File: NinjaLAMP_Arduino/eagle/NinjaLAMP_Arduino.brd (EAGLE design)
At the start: 50.8 x 33 mm, 13 parts

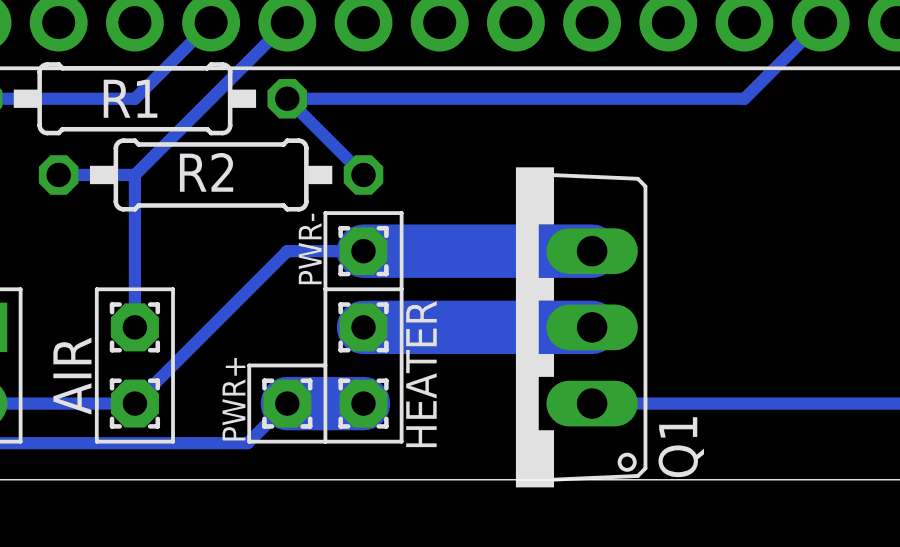
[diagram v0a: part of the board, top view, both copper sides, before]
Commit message: update 3d model : add cover
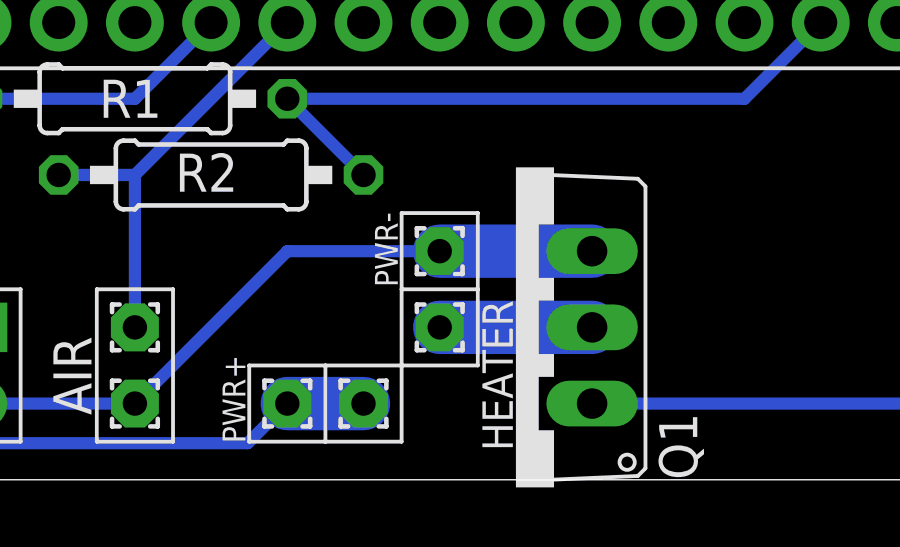
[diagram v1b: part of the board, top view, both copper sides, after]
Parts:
- moved HEATER2 2.54 mm to (20.3, 5.08)
- moved POWER- 2.54 mm to (20.3, 7.62)
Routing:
- net DRAIN: track 7.62 -> 5.08 mm
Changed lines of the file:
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@@
 <setting verticaltext="up"/>
 </settings>
-<grid distance="1" unitdist="mil" unit="mil" style="lines" multiple="1" display="yes" altdistance="5" altunitdist="mil" altunit="mil"/>
+<grid distance="50" unitdist="mil" unit="mil" style="lines" multiple="1" display="yes" altdistance="5" altunitdist="mil" altunit="mil"/>
 <layers>
 <layer number="1" name="Top" color="4" fill="1" visible="yes" active="yes"/>
@@
 <text x="3.556" y="1.4732" size="1.27" layer="25" rot="R90">WELL</text>
 <text x="8.7122" y="2.159" size="1.27" layer="25" rot="R90">AIR</text>
-<text x="16.383" y="6.4262" size="0.762" layer="25" rot="R90">PWR-</text>
-<text x="20.2184" y="0.9652" size="1.016" layer="25" rot="R90">HEATER</text>
+<text x="18.923" y="6.4262" size="0.762" layer="25" rot="R90">PWR-</text>
+<text x="22.7584" y="0.9652" size="1.016" layer="25" rot="R90">HEATER</text>
 <wire x1="8.89" y1="6.35" x2="8.89" y2="1.27" width="0.127" layer="21"/>
 <wire x1="8.89" y1="1.27" x2="11.43" y2="1.27" width="0.127" layer="21"/>
@@
 <wire x1="11.43" y1="1.27" x2="11.43" y2="6.35" width="0.127" layer="21"/>
 <wire x1="16.51" y1="1.27" x2="19.05" y2="1.27" width="0.127" layer="21"/>
-<wire x1="19.05" y1="1.27" x2="19.05" y2="6.35" width="0.127" layer="21"/>
-<wire x1="19.05" y1="6.35" x2="16.51" y2="6.35" width="0.127" layer="21"/>
-<wire x1="16.51" y1="6.35" x2="16.51" y2="3.81" width="0.127" layer="21"/>
+<wire x1="19.05" y1="1.27" x2="19.05" y2="3.81" width="0.127" layer="21"/>
+<wire x1="19.05" y1="3.81" x2="19.05" y2="6.35" width="0.127" layer="21"/>
 <wire x1="16.51" y1="3.81" x2="16.51" y2="1.27" width="0.127" layer="21"/>
 <wire x1="12.7" y1="22.86" x2="2.54" y2="22.86" width="0.127" layer="21"/>
@@
 <wire x1="13.97" y1="1.27" x2="13.97" y2="3.81" width="0.127" layer="21"/>
 <wire x1="13.97" y1="3.81" x2="16.51" y2="3.81" width="0.127" layer="21"/>
-<wire x1="16.51" y1="6.35" x2="16.51" y2="8.89" width="0.127" layer="21"/>
-<wire x1="16.51" y1="8.89" x2="19.05" y2="8.89" width="0.127" layer="21"/>
-<wire x1="19.05" y1="8.89" x2="19.05" y2="6.35" width="0.127" layer="21"/>
 <text x="13.843" y="1.2192" size="0.762" layer="25" rot="R90">PWR+</text>
+<wire x1="19.05" y1="8.89" x2="21.59" y2="8.89" width="0.127" layer="21"/>
+<wire x1="21.59" y1="8.89" x2="21.59" y2="6.35" width="0.127" layer="21"/>
+<wire x1="21.59" y1="6.35" x2="19.05" y2="6.35" width="0.127" layer="21"/>
+<wire x1="19.05" y1="6.35" x2="19.05" y2="8.89" width="0.127" layer="21"/>
+<wire x1="16.51" y1="3.81" x2="19.05" y2="3.81" width="0.127" layer="21"/>
+<wire x1="19.05" y1="3.81" x2="21.59" y2="3.81" width="0.127" layer="21"/>
+<wire x1="21.59" y1="3.81" x2="21.59" y2="6.35" width="0.127" layer="21"/>
 </plain>
 <attributes>
@@
 <attribute name="VALUE" x="17.78" y="3.14" size="0.0254" layer="27"/>
 </element>
-<element name="HEATER2" library="wirepad" library_urn="urn:adsk.eagle:library:412" package="1,6/0,8" package3d_urn="urn:adsk.eagle:package:30830/1" value="" x="17.78" y="5.08" smashed="yes">
-<attribute name="POPULARITY" value="15" x="39.37" y="-31.75" size="1.778" layer="27" display="off"/>
-<attribute name="VALUE" x="17.78" y="5.68" size="0.0254" layer="27"/>
+<element name="HEATER2" library="wirepad" library_urn="urn:adsk.eagle:library:412" package="1,6/0,8" package3d_urn="urn:adsk.eagle:package:30830/1" value="" x="20.32" y="5.08" smashed="yes">
+<attribute name="POPULARITY" value="15" x="41.91" y="-31.75" size="1.778" layer="27" display="off"/>
+<attribute name="VALUE" x="20.32" y="5.68" size="0.0254" layer="27"/>
 </element>
 <element name="NTC_AIR1" library="wirepad" library_urn="urn:adsk.eagle:library:412" package="1,6/0,8" package3d_urn="urn:adsk.eagle:package:30830/1" value="" x="10.16" y="5.08" smashed="yes">
@@
 <attribute name="VALUE" x="15.24" y="3.14" size="0.0254" layer="27"/>
 </element>
-<element name="POWER-" library="wirepad" library_urn="urn:adsk.eagle:library:412" package="1,6/0,8" package3d_urn="urn:adsk.eagle:package:30830/1" value="" x="17.78" y="7.62" smashed="yes">
-<attribute name="POPULARITY" value="15" x="17.78" y="7.62" size="1.778" layer="27" display="off"/>
-<attribute name="VALUE" x="17.78" y="8.22" size="0.0254" layer="27"/>
+<element name="POWER-" library="wirepad" library_urn="urn:adsk.eagle:library:412" package="1,6/0,8" package3d_urn="urn:adsk.eagle:package:30830/1" value="" x="20.32" y="7.62" smashed="yes">
+<attribute name="POPULARITY" value="15" x="20.32" y="7.62" size="1.778" layer="27" display="off"/>
+<attribute name="VALUE" x="20.32" y="8.22" size="0.0254" layer="27"/>
 </element>
 </elements>
@@
 <wire x1="7.62" y1="20.32" x2="33.02" y2="20.32" width="0.4064" layer="16"/>
 <wire x1="5.08" y1="2.54" x2="10.16" y2="2.54" width="0.4064" layer="16"/>
-<wire x1="17.78" y1="7.62" x2="25.4" y2="7.62" width="1.778" layer="16"/>
-<wire x1="17.78" y1="7.62" x2="15.24" y2="7.62" width="0.4064" layer="16"/>
+<wire x1="20.32" y1="7.62" x2="25.4" y2="7.62" width="1.778" layer="16"/>
+<wire x1="20.32" y1="7.62" x2="15.24" y2="7.62" width="0.4064" layer="16"/>
 <wire x1="15.24" y1="7.62" x2="10.16" y2="2.54" width="0.4064" layer="16"/>
 </signal>
@@
 <contactref element="Q1" pad="2"/>
 <contactref element="HEATER2" pad="1"/>
-<wire x1="17.78" y1="5.08" x2="25.4" y2="5.08" width="1.778" layer="16"/>
+<wire x1="20.32" y1="5.08" x2="25.4" y2="5.08" width="1.778" layer="16"/>
 </signal>
 </signals>
